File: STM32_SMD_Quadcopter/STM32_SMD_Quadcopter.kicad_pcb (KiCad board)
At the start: 2 copper layers, 36.5 x 25.4 mm, 64 parts, among them J1 PWR, J2 USB_B_Micro, J3 Micro_SD_Card_Det, J4 DEBUG, J5 DSMX, M1 Brushed_DC, M2 Brushed_DC, M3 Brushed_DC, M4 Brushed_DC, Q1 IRLML6244TR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

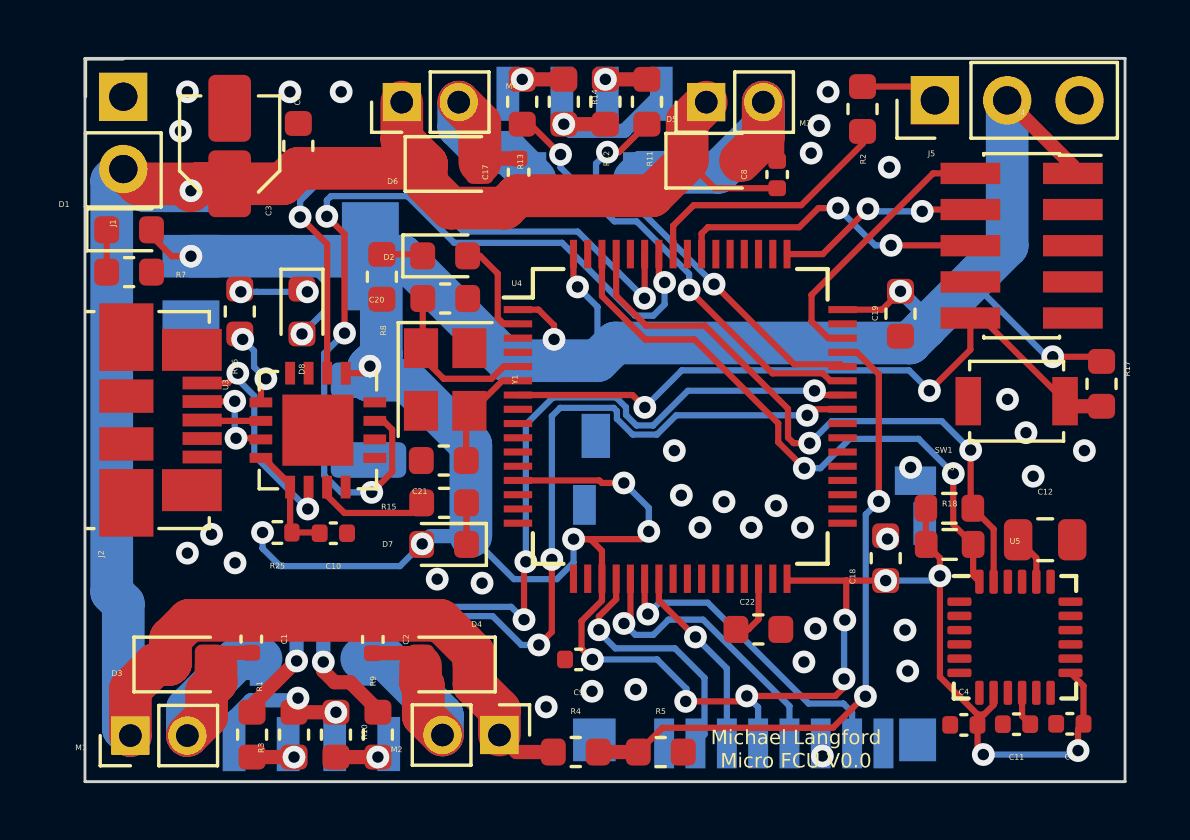
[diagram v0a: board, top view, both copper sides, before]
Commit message: Finished and almost ready for purchase, with stm32f446RET6 and FT230XQ
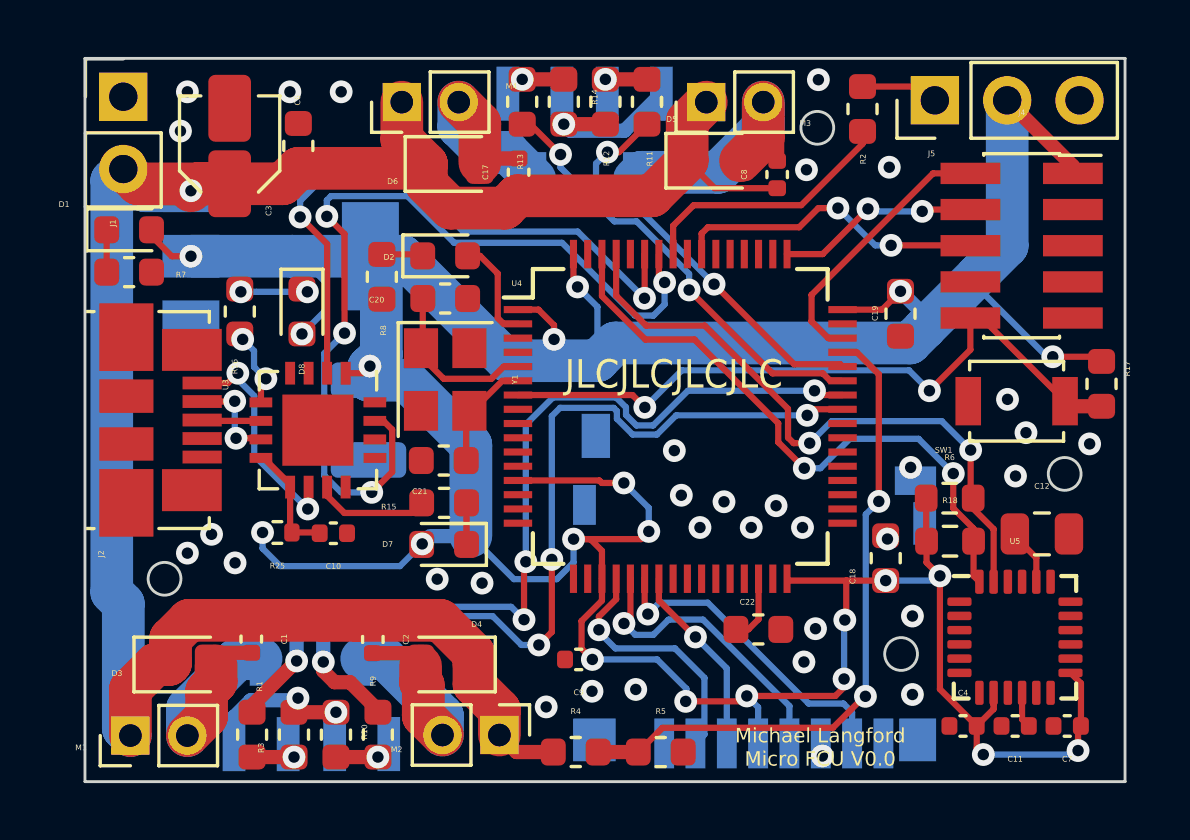
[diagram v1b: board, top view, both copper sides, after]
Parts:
- moved R6 0.36 mm to (78.3, 43.4)
- moved C12 0.23 mm to (81.5, 44.7)
- moved C7 0.12 mm to (82.4, 51.4)
- moved R18 0.12 mm to (78.3, 44.9)
- moved C11 0.08 mm to (80.6, 51.4)
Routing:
- net +3V3: track 142.2 -> 143.2 mm
- net GND: vias 37 -> 36
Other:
- outline, holes or cut-outs redrawn
- board text added: "JLCJLCJLCJLC"
